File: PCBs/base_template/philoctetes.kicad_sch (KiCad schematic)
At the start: 174 parts, among them U1 TRRS, U2 TRRS, sw1 Keyswitch, sw10 Keyswitch, sw11 Keyswitch, sw12 Keyswitch, sw13 Keyswitch, sw14 Keyswitch, sw15 Keyswitch, sw16 Keyswitch, sw17 Keyswitch, sw18 Keyswitch, sw19 Keyswitch, sw2 Keyswitch, sw20 Keyswitch, sw21 Keyswitch, sw22 Keyswitch, sw23 Keyswitch, sw24 Keyswitch, sw25 Keyswitch, sw26 Keyswitch, sw27 Keyswitch, sw28 Keyswitch, sw29 Keyswitch, sw3 Keyswitch, sw30 Keyswitch, sw31 Keyswitch, sw32 Keyswitch, sw33 Keyswitch, sw34 Keyswitch, sw35 Keyswitch, sw36 Keyswitch, sw37 Keyswitch, sw38 Keyswitch, sw39 Keyswitch, sw4 Keyswitch, sw40 Keyswitch, sw41 Keyswitch, sw42 Keyswitch, sw5 Keyswitch, sw6 Keyswitch, sw7 Keyswitch, sw8 Keyswitch, sw9 Keyswitch

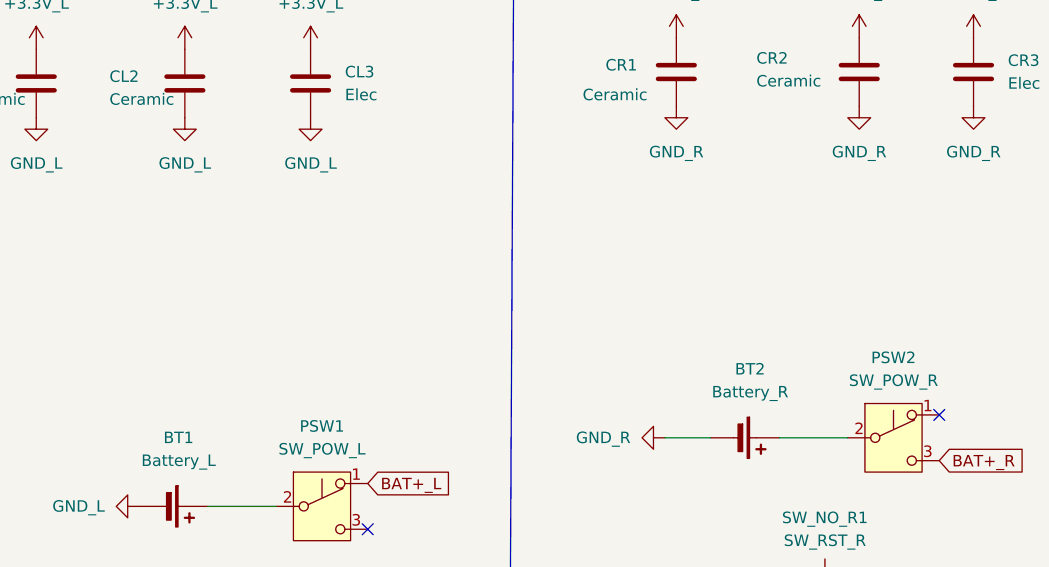
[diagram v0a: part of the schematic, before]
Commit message: layout right side improvements
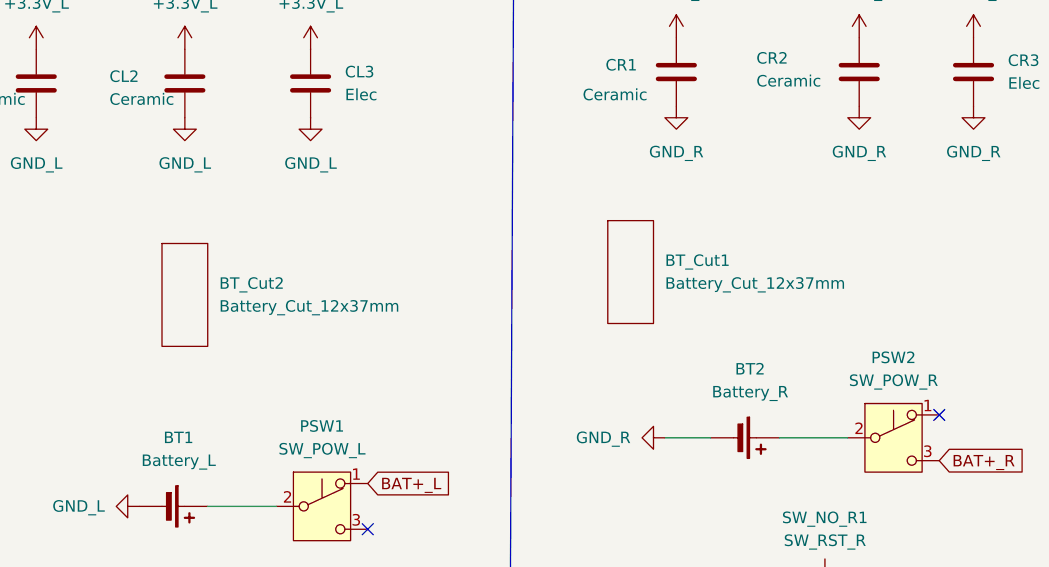
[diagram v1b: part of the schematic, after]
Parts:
- added BT_Cut1, BT_Cut2: Battery_Cut_12x37mm, philoctetes:Battery_Cut_12x37mm, symbol philoctetes:Battery_Cut_12x37mm
- CL3, CR3: footprint Capacitor_SMD:CP_Elec_5x5.4 -> philoctetes:CP_Radial_D5.0mm_P2.00mm
- D1, D10, D11, D12, D13, D14, D15, D16, D17, D18, D19, D2, D20, D21, D3, D4, D5, D6, D7, D8, D9: footprint Diode_SMD:D_SOD-323 -> Diode_SMD:D_SOD-123F
- DL10, DL11, DL12, DL13, DL14, DL15, DL16, DL17, DL18, DL19, DL2, DL20, DL21, DL3, DL4, DL5, DL6, DL7, DL8, DL9: footprint Diode_SMD:D_SOD-323_HandSoldering -> Diode_SMD:D_SOD-123F
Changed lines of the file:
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@@
 (kicad_sch
-	(version 20231120)
+	(version 20250114)
 	(generator "eeschema")
-	(generator_version "8.0")
+	(generator_version "9.0")
 	(paper "A3")
 	(title_block
@@
 		(company "License: CERN-OHL-S")
 	)
+	(text "PHILOCTETES KEYBOARD"
+		(exclude_from_sim no)
+		(at 128.524 269.24 0)
+		(effects
+			(font
+				(size 12 12)
+			)
+		)
+	)
 	(junction
 		(at 284.48 219.71)
@@
 		)
 	)
-	(text "PHILOCTETES KEYBOARD"
-		(exclude_from_sim no)
-		(at 128.524 269.24 0)
-		(effects
-			(font
-				(size 12 12)
-			)
-		)
-	)
 	(global_label "col2_L"
 		(shape input)
@@
 			)
 		)
-		(property "Footprint" "Diode_SMD:D_SOD-323_HandSoldering"
+		(property "Footprint" "Diode_SMD:D_SOD-123F"
 			(at 133.35 47.625 0)
 			(effects
@@
 			)
 		)
-		(property "Footprint" "Diode_SMD:D_SOD-323_HandSoldering"
+		(property "Footprint" "Diode_SMD:D_SOD-123F"
 			(at 111.76 86.995 0)
 			(effects
@@
 			)
 		)
-		(property "Footprint" "Diode_SMD:D_SOD-323_HandSoldering"
+		(property "Footprint" "Diode_SMD:D_SOD-123F"
 			(at 55.88 28.575 0)
 			(effects
@@
 			)
 		)
-		(property "Footprint" "Diode_SMD:D_SOD-323"
+		(property "Footprint" "Diode_SMD:D_SOD-123F"
 			(at 294.64 32.385 0)
 			(effects
@@
 			)
 		)
-		(property "Footprint" "Diode_SMD:D_SOD-323"
+		(property "Footprint" "Diode_SMD:D_SOD-123F"
 			(at 389.89 70.485 0)
 			(effects
@@
 			)
 		)
-		(property "Footprint" "Diode_SMD:D_SOD-323_HandSoldering"
+		(property "Footprint" "Diode_SMD:D_SOD-123F"
 			(at 133.35 28.575 0)
 			(effects
@@
 			)
 		)
-		(property "Footprint" "Diode_SMD:D_SOD-323_HandSoldering"
+		(property "Footprint" "Diode_SMD:D_SOD-123F"
 			(at 111.76 47.625 0)
 			(effects
@@
 			)
 		)
-		(property "Footprint" "Diode_SMD:D_SOD-323"
+		(property "Footprint" "Diode_SMD:D_SOD-123F"
 			(at 294.64 70.485 0)
 			(effects
@@
 			)
 		)
-		(property "Footprint" "Diode_SMD:D_SOD-323"
+		(property "Footprint" "Diode_SMD:D_SOD-123F"
 			(at 312.42 32.385 0)
 			(effects
@@
 			)
 		)
-		(property "Footprint" "Diode_SMD:D_SOD-323_HandSoldering"
+		(property "Footprint" "Diode_SMD:D_SOD-123F"
 			(at 91.44 66.675 0)
 			(effects
@@
 			)
 		)
-		(property "Footprint" "Diode_SMD:D_SOD-323_HandSoldering"
+		(property "Footprint" "Diode_SMD:D_SOD-123F"
 			(at 91.44 86.995 0)
 			(effects
@@
 			)
 		)
-		(property "Footprint" "Diode_SMD:D_SOD-323_HandSoldering"
+		(property "Footprint" "Diode_SMD:D_SOD-123F"
 			(at 55.88 47.625 0)
 			(effects
@@
 			)
 		)
-		(property "Footprint" "Diode_SMD:D_SOD-323"
+		(property "Footprint" "Diode_SMD:D_SOD-123F"
 			(at 312.42 86.995 0)
 			(effects
@@
 			)
 		)
-		(property "Footprint" "Diode_SMD:D_SOD-323"
+		(property "Footprint" "Diode_SMD:D_SOD-123F"
 			(at 330.2 51.435 0)
 			(effects
@@
 			)
 		)
-		(property "Footprint" "Diode_SMD:D_SOD-323_HandSoldering"
+		(property "Footprint" "Diode_SMD:D_SOD-123F"
 			(at 133.35 86.995 0)
 			(effects
@@
 			)
 		)
-		(property "Footprint" "Diode_SMD:D_SOD-323_HandSoldering"
+		(property "Footprint" "Diode_SMD:D_SOD-123F"
 			(at 91.44 28.575 0)
 			(effects
@@
 			)
 		)
-		(property "Footprint" "Diode_SMD:D_SOD-323_HandSoldering"
+		(property "Footprint" "Diode_SMD:D_SOD-123F"
 			(at 133.35 66.675 0)
 			(effects
@@
 			)
 		)
-		(property "Footprint" "Diode_SMD:D_SOD-323"
+		(property "Footprint" "Diode_SMD:D_SOD-123F"
 			(at 294.64 86.995 0)
 			(effects
@@
 			)
 		)
-		(property "Footprint" "Diode_SMD:D_SOD-323"
+		(property "Footprint" "Diode_SMD:D_SOD-123F"
 			(at 389.89 32.385 0)
 			(effects
@@
 			)
 		)
-		(property "Footprint" "Diode_SMD:D_SOD-323_HandSoldering"
+		(property "Footprint" "Diode_SMD:D_SOD-123F"
 			(at 38.1 47.625 0)
 			(effects
@@
 			)
 		)
-		(property "Footprint" "Diode_SMD:D_SOD-323_HandSoldering"
+		(property "Footprint" "Diode_SMD:D_SOD-123F"
 			(at 73.66 28.575 0)
 			(effects
@@
 			)
 		)
-		(property "Footprint" "Diode_SMD:D_SOD-323"
+		(property "Footprint" "Diode_SMD:D_SOD-123F"
 			(at 330.2 32.385 0)
 			(effects
@@
 			)
 		)
-		(property "Footprint" "Diode_SMD:D_SOD-323"
+		(property "Footprint" "Diode_SMD:D_SOD-123F"
 			(at 312.42 70.485 0)
 			(effects
@@
 			)
 		)
-		(property "Footprint" "Diode_SMD:D_SOD-323"
+		(property "Footprint" "Diode_SMD:D_SOD-123F"
 			(at 330.2 86.995 0)
 			(effects
@@
 			)
 		)
-		(property "Footprint" "Diode_SMD:D_SOD-323"
+		(property "Footprint" "Diode_SMD:D_SOD-123F"
 			(at 368.3 32.385 0)
 			(effects
@@
 	)
 	(symbol
+		(lib_id "philoctetes:Battery_Cut_12x37mm")
+		(at 176.53 105.41 0)
+		(unit 1)
+		(exclude_from_sim no)
+		(in_bom yes)
+		(on_board yes)
+		(dnp no)
+		(fields_autoplaced yes)
+		(property "Reference" "BT_Cut2"
+			(at 180.34 103.5049 0)
+			(effects
+				(font
+					(size 1.27 1.27)
+				)
+				(justify left)
+			)
+		)
+		(property "Value" "Battery_Cut_12x37mm"
+			(at 180.34 106.0449 0)
+			(effects
+				(font
+					(size 1.27 1.27)
+				)
+				(justify left)
+			)
+		)
+		(property "Footprint" "philoctetes:Battery_Cut_12x37mm"
+			(at 195.834 112.014 0)
+			(effects
+				(font
+					(size 1.27 1.27)
+				)
+				(hide yes)
+			)
+		)
+		(property "Datasheet" "kicad-embed://194mAh_battery.pdf"
+			(at 176.53 103.886 90)
+			(effects
+				(font
+					(size 1.27 1.27)
+				)
+				(hide yes)
+			)
+		)
+		(property "Description" "Single-cell battery"
+			(at 189.738 109.728 0)
+			(effects
+				(font
+					(size 1.27 1.27)
+				)
+				(hide yes)
+			)
+		)
+		(instances
+			(project ""
+				(path "/2a55be96-0621-414c-9e2a-5e2757c4c7b6"
+					(reference "BT_Cut2")
+					(unit 1)
+				)
+			)
+		)
+	)
+	(symbol
 		(lib_id "power:GND")
 		(at 187.96 160.02 180)
@@
 	)
 	(symbol
+		(lib_id "philoctetes:Battery_Cut_12x37mm")
+		(at 226.06 102.87 0)
+		(unit 1)
+		(exclude_from_sim no)
+		(in_bom yes)
+		(on_board yes)
+		(dnp no)
+		(fields_autoplaced yes)
+		(property "Reference" "BT_Cut1"
+			(at 229.87 100.9649 0)
+			(effects
+				(font
+					(size 1.27 1.27)
+				)
+				(justify left)
+			)
+		)
+		(property "Value" "Battery_Cut_12x37mm"
+			(at 229.87 103.5049 0)
+			(effects
+				(font
+					(size 1.27 1.27)
+				)
+				(justify left)
+			)
+		)
+		(property "Footprint" "philoctetes:Battery_Cut_12x37mm"
+			(at 245.364 109.474 0)
+			(effects
+				(font
+					(size 1.27 1.27)
+				)
+				(hide yes)
+			)
+		)
+		(property "Datasheet" "kicad-embed://194mAh_battery.pdf"
+			(at 226.06 101.346 90)
+			(effects
+				(font
+					(size 1.27 1.27)
+				)
+				(hide yes)
+			)
+		)
+		(property "Description" "Single-cell battery"
+			(at 239.268 107.188 0)
+			(effects
+				(font
+					(size 1.27 1.27)
+				)
+				(hide yes)
+			)
+		)
+		(instances
+			(project ""
+				(path "/2a55be96-0621-414c-9e2a-5e2757c4c7b6"
+					(reference "BT_Cut1")
+					(unit 1)
+				)
+			)
+		)
+	)
+	(symbol
 		(lib_name "SK6821MINI-E_facedown_25")
 		(lib_id "philoctetes:SK6821MINI-E_facedown")
@@
 			)
 		)
-		(property "Footprint" "Diode_SMD:D_SOD-323"
+		(property "Footprint" "Diode_SMD:D_SOD-123F"
 			(at 330.2 70.485 0)
 			(effects
@@
 			)
 		)
-		(property "Footprint" "Diode_SMD:D_SOD-323_HandSoldering"
+		(property "Footprint" "Diode_SMD:D_SOD-123F"
 			(at 73.66 47.625 0)
 			(effects
@@
 			)
 		)
-		(property "Footprint" "Diode_SMD:D_SOD-323_HandSoldering"
+		(property "Footprint" "Diode_SMD:D_SOD-123F"
 			(at 38.1 66.675 0)
 			(effects
@@
 			)
 		)
-		(property "Footprint" "Diode_SMD:D_SOD-323"
+		(property "Footprint" "Diode_SMD:D_SOD-123F"
 			(at 347.98 70.485 0)
 			(effects
@@
 			)
 		)
-		(property "Footprint" "Diode_SMD:D_SOD-323_HandSoldering"
+		(property "Footprint" "Diode_SMD:D_SOD-123F"
 			(at 91.44 47.625 0)
 			(effects
@@
 			)
 		)
-		(property "Footprint" "Diode_SMD:D_SOD-323"
+		(property "Footprint" "Diode_SMD:D_SOD-123F"
 			(at 347.98 32.385 0)
 			(effects
@@
 			)
 		)
-		(property "Footprint" "Diode_SMD:D_SOD-323"
+		(property "Footprint" "Diode_SMD:D_SOD-123F"
 			(at 389.89 51.435 0)
 			(effects
@@
 			)
 		)
-		(property "Footprint" "Diode_SMD:D_SOD-323_HandSoldering"
+		(property "Footprint" "Diode_SMD:D_SOD-123F"
 			(at 73.66 66.675 0)
 			(effects
@@
 			)
 		)
-		(property "Footprint" "Diode_SMD:D_SOD-323_HandSoldering"
+		(property "Footprint" "Diode_SMD:D_SOD-123F"
 			(at 111.76 66.675 0)
 			(effects
@@
 			)
 		)
-		(property "Footprint" "Diode_SMD:D_SOD-323_HandSoldering"
+		(property "Footprint" "Diode_SMD:D_SOD-123F"
 			(at 55.88 66.675 0)
 			(effects
@@
 			)
 		)
-		(property "Footprint" "Capacitor_SMD:CP_Elec_5x5.4"
+		(property "Footprint" "philoctetes:CP_Radial_D5.0mm_P2.00mm"
 			(at 265.1252 83.82 0)
 			(effects
@@
 			)
 		)
-		(property "Footprint" "Capacitor_SMD:CP_Elec_5x5.4"
+		(property "Footprint" "philoctetes:CP_Radial_D5.0mm_P2.00mm"
 			(at 191.4652 85.09 0)
 			(effects
@@
 			)
 		)
-		(property "Footprint" "Diode_SMD:D_SOD-323_HandSoldering"
+		(property "Footprint" "Diode_SMD:D_SOD-123F"
 			(at 111.76 28.575 0)
 			(effects
@@
 			)
 		)
-		(property "Footprint" "Diode_SMD:D_SOD-323"
+		(property "Footprint" "Diode_SMD:D_SOD-123F"
 			(at 368.3 51.435 0)
 			(effects
@@
 			)
 		)
-		(property "Footprint" "Diode_SMD:D_SOD-323"
+		(property "Footprint" "Diode_SMD:D_SOD-123F"
 			(at 294.64 51.435 0)
 			(effects
@@
 			)
 		)
-		(property "Footprint" "Diode_SMD:D_SOD-323"
+		(property "Footprint" "Diode_SMD:D_SOD-123F"
 			(at 312.42 51.435 0)
 			(effects
@@
 			)
 		)
-		(property "Footprint" "Diode_SMD:D_SOD-323"
+		(property "Footprint" "Diode_SMD:D_SOD-123F"
 			(at 368.3 70.485 0)
 			(effects
@@
 			)
 		)
-		(property "Footprint" "Diode_SMD:D_SOD-323"
+		(property "Footprint" "Diode_SMD:D_SOD-123F"
 			(at 347.98 51.435 0)
 			(effects
@@
 		)
 	)
+	(embedded_fonts no)
 )

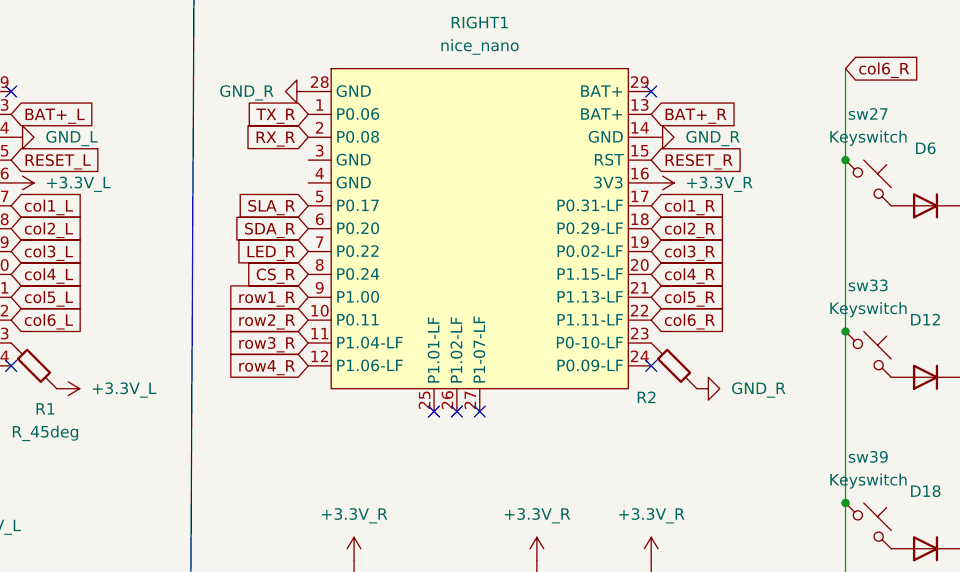
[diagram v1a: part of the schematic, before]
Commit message: routing right half; diodes, power, reset, tx, rx, clk...
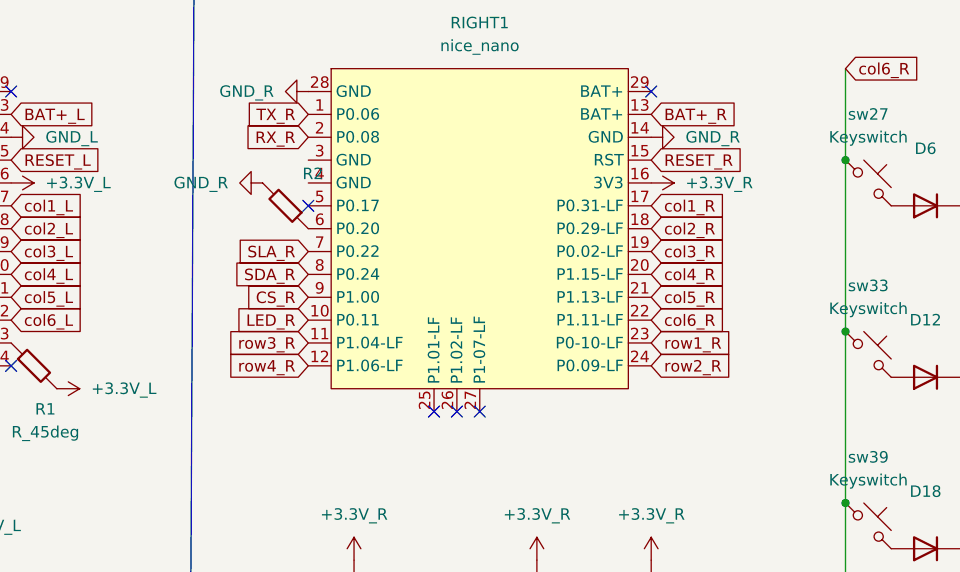
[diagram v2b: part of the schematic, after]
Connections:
- net CS_R: now also RIGHT1.9 (P1.00); no longer RIGHT1.8 (P0.24)
- net LED_R: now also RIGHT1.10 (P0.11); no longer RIGHT1.7 (P0.22)
- net SDA_R: now also RIGHT1.8 (P0.24); no longer RIGHT1.6 (P0.20)
- net SLA_R: now also RIGHT1.7 (P0.22); no longer RIGHT1.5 (P0.17)
- net row1_R: now also RIGHT1.23 (P0-10-LF); no longer RIGHT1.9 (P1.00)
- net row2_R: now also RIGHT1.24 (P0.09-LF); no longer RIGHT1.10 (P0.11)
- net at R2.1: now also RIGHT1.6 (P0.20); no longer RIGHT1.23 (P0-10-LF)
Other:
- moved on the sheet: R2
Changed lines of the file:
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@@
 	)
 	(no_connect
-		(at 264.16 54.61)
+		(at 226.06 36.83)
 	)
 	(no_connect
@@
 	(global_label "LED_R"
 		(shape input)
-		(at 226.06 41.91 180)
+		(at 226.06 49.53 180)
 		(fields_autoplaced yes)
 		(effects
@@
 		)
 		(property "Intersheetrefs" "${INTERSHEET_REFS}"
-			(at 217.3901 41.91 0)
+			(at 217.3901 49.53 0)
 			(effects
 				(font
@@
 	(global_label "CS_R"
 		(shape input)
-		(at 226.06 44.45 180)
+		(at 226.06 46.99 180)
 		(fields_autoplaced yes)
 		(effects
@@
 		)
 		(property "Intersheetrefs" "${INTERSHEET_REFS}"
-			(at 218.3577 44.45 0)
+			(at 218.3577 46.99 0)
 			(effects
 				(font
@@
 	(global_label "row1_R"
 		(shape input)
-		(at 226.06 46.99 180)
+		(at 264.16 52.07 0)
 		(fields_autoplaced yes)
 		(effects
@@
 				(size 1.27 1.27)
 			)
-			(justify right)
+			(justify left)
 		)
 		(property "Intersheetrefs" "${INTERSHEET_REFS}"
-			(at 216.362 46.99 0)
+			(at 273.858 52.07 0)
 			(effects
 				(font
 					(size 1.27 1.27)
 				)
-				(justify right)
+				(justify left)
 				(hide yes)
 			)
@@
 	(global_label "SDA_R"
 		(shape input)
-		(at 226.06 39.37 180)
+		(at 226.06 44.45 180)
 		(fields_autoplaced yes)
 		(effects
@@
 		)
 		(property "Intersheetrefs" "${INTERSHEET_REFS}"
-			(at 217.2691 39.37 0)
+			(at 217.2691 44.45 0)
 			(effects
 				(font
@@
 	(global_label "SLA_R"
 		(shape input)
-		(at 226.06 36.83 180)
+		(at 226.06 41.91 180)
 		(fields_autoplaced yes)
 		(effects
@@
 		)
 		(property "Intersheetrefs" "${INTERSHEET_REFS}"
-			(at 217.511 36.83 0)
+			(at 217.511 41.91 0)
 			(effects
 				(font
@@
 	(global_label "row2_R"
 		(shape input)
-		(at 226.06 49.53 180)
+		(at 264.16 54.61 0)
 		(fields_autoplaced yes)
 		(effects
@@
 				(size 1.27 1.27)
 			)
-			(justify right)
+			(justify left)
 		)
 		(property "Intersheetrefs" "${INTERSHEET_REFS}"
-			(at 216.362 49.53 0)
+			(at 273.858 54.61 0)
 			(effects
 				(font
 					(size 1.27 1.27)
 				)
-				(justify right)
+				(justify left)
 				(hide yes)
 			)
@@
 	)
 	(symbol
+		(lib_id "power:GND")
+		(at 220.98 34.29 270)
+		(unit 1)
+		(exclude_from_sim no)
+		(in_bom yes)
+		(on_board yes)
+		(dnp no)
+		(fields_autoplaced yes)
+		(property "Reference" "#PWR050"
+			(at 214.63 34.29 0)
+			(effects
+				(font
+					(size 1.27 1.27)
+				)
+				(hide yes)
+			)
+		)
+		(property "Value" "GND_R"
+			(at 217.17 34.2899 90)
+			(effects
+				(font
+					(size 1.27 1.27)
+				)
+				(justify right)
+			)
+		)
+		(property "Footprint" ""
+			(at 220.98 34.29 0)
+			(effects
+				(font
+					(size 1.27 1.27)
+				)
+				(hide yes)
+			)
+		)
+		(property "Datasheet" ""
+			(at 220.98 34.29 0)
+			(effects
+				(font
+					(size 1.27 1.27)
+				)
+				(hide yes)
+			)
+		)
+		(property "Description" "Power symbol creates a global label with name \"GND\" , ground"
+			(at 220.98 34.29 0)
+			(effects
+				(font
+					(size 1.27 1.27)
+				)
+				(hide yes)
+			)
+		)
+		(pin "1"
+		)
+		(instances
+			(project "philoctetes"
+				(path "/2a55be96-0621-414c-9e2a-5e2757c4c7b6"
+					(reference "#PWR050")
+					(unit 1)
+				)
+			)
+		)
+	)
+	(symbol
 		(lib_id "power:+3.3V")
 		(at 198.12 57.15 270)
@@
 	)
 	(symbol
-		(lib_id "power:GND")
-		(at 269.24 57.15 90)
-		(unit 1)
-		(exclude_from_sim no)
-		(in_bom yes)
-		(on_board yes)
-		(dnp no)
-		(fields_autoplaced yes)
-		(property "Reference" "#PWR050"
-			(at 275.59 57.15 0)
-			(effects
-				(font
-					(size 1.27 1.27)
-				)
-				(hide yes)
-			)
-		)
-		(property "Value" "GND_R"
-			(at 273.05 57.1499 90)
-			(effects
-				(font
-					(size 1.27 1.27)
-				)
-				(justify right)
-			)
-		)
-		(property "Footprint" ""
-			(at 269.24 57.15 0)
-			(effects
-				(font
-					(size 1.27 1.27)
-				)
-				(hide yes)
-			)
-		)
-		(property "Datasheet" ""
-			(at 269.24 57.15 0)
-			(effects
-				(font
-					(size 1.27 1.27)
-				)
-				(hide yes)
-			)
-		)
-		(property "Description" "Power symbol creates a global label with name \"GND\" , ground"
-			(at 269.24 57.15 0)
-			(effects
-				(font
-					(size 1.27 1.27)
-				)
-				(hide yes)
-			)
-		)
-		(pin "1"
-		)
-		(instances
-			(project "philoctetes"
-				(path "/2a55be96-0621-414c-9e2a-5e2757c4c7b6"
-					(reference "#PWR050")
-					(unit 1)
-				)
-			)
-			(project "mysuperawesomekb_right"
-				(path "/4a04f5f3-f5f7-4d2e-9596-22b42a392671"
-					(reference "#PWR01")
-					(unit 1)
-				)
-			)
-		)
-	)
-	(symbol
 		(lib_id "home:Placeholder_Keyswitch")
 		(at 288.29 53.34 0)
@@
 	(symbol
 		(lib_id "Device:R_45deg")
-		(at 266.7 54.61 0)
+		(at 223.52 36.83 180)
 		(unit 1)
 		(exclude_from_sim no)
@@
 		(dnp no)
 		(property "Reference" "R2"
-			(at 263.652 58.166 0)
+			(at 226.568 33.274 0)
 			(effects
 				(font
@@
 		)
 		(property "Value" "R_45deg"
-			(at 265.684 58.674 0)
+			(at 224.536 32.766 0)
 			(effects
 				(font
@@
 		)
 		(property "Footprint" "Resistor_SMD:R_0805_2012Metric"
-			(at 266.7 56.388 0)
+			(at 223.52 35.052 0)
 			(effects
 				(font
@@
 		)
 		(property "Datasheet" "~"
-			(at 266.7 54.61 0)
+			(at 223.52 36.83 0)
 			(effects
 				(font
@@
 		)
 		(property "Description" "Resistor, rotated by 45°"
-			(at 266.7 54.61 0)
+			(at 223.52 36.83 0)
 			(effects
 				(font
